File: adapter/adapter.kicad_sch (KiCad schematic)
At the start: 22 parts, among them J1 Serial, J10 Ribbon, J3 Battery charge, J4 RGB, J9 Ribbon, SW1 SW_SPST, SW3 SW_SPDT, U1 Dual MCU: RP2040 + nice!nano, U2 AP1603WG-7

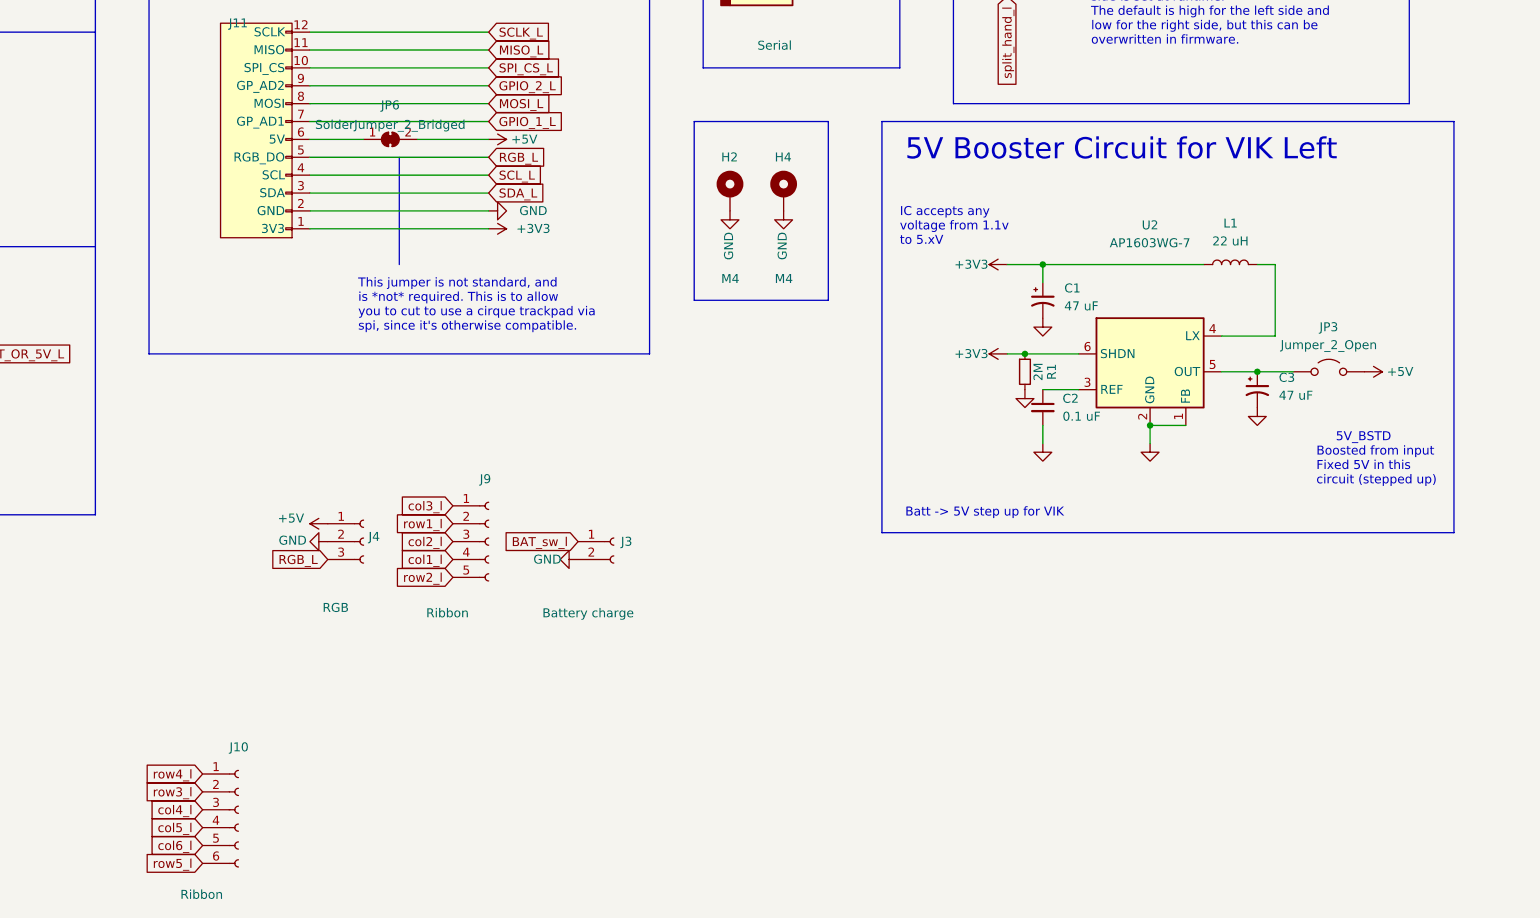
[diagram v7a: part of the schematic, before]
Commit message: sch: remove booster circuit
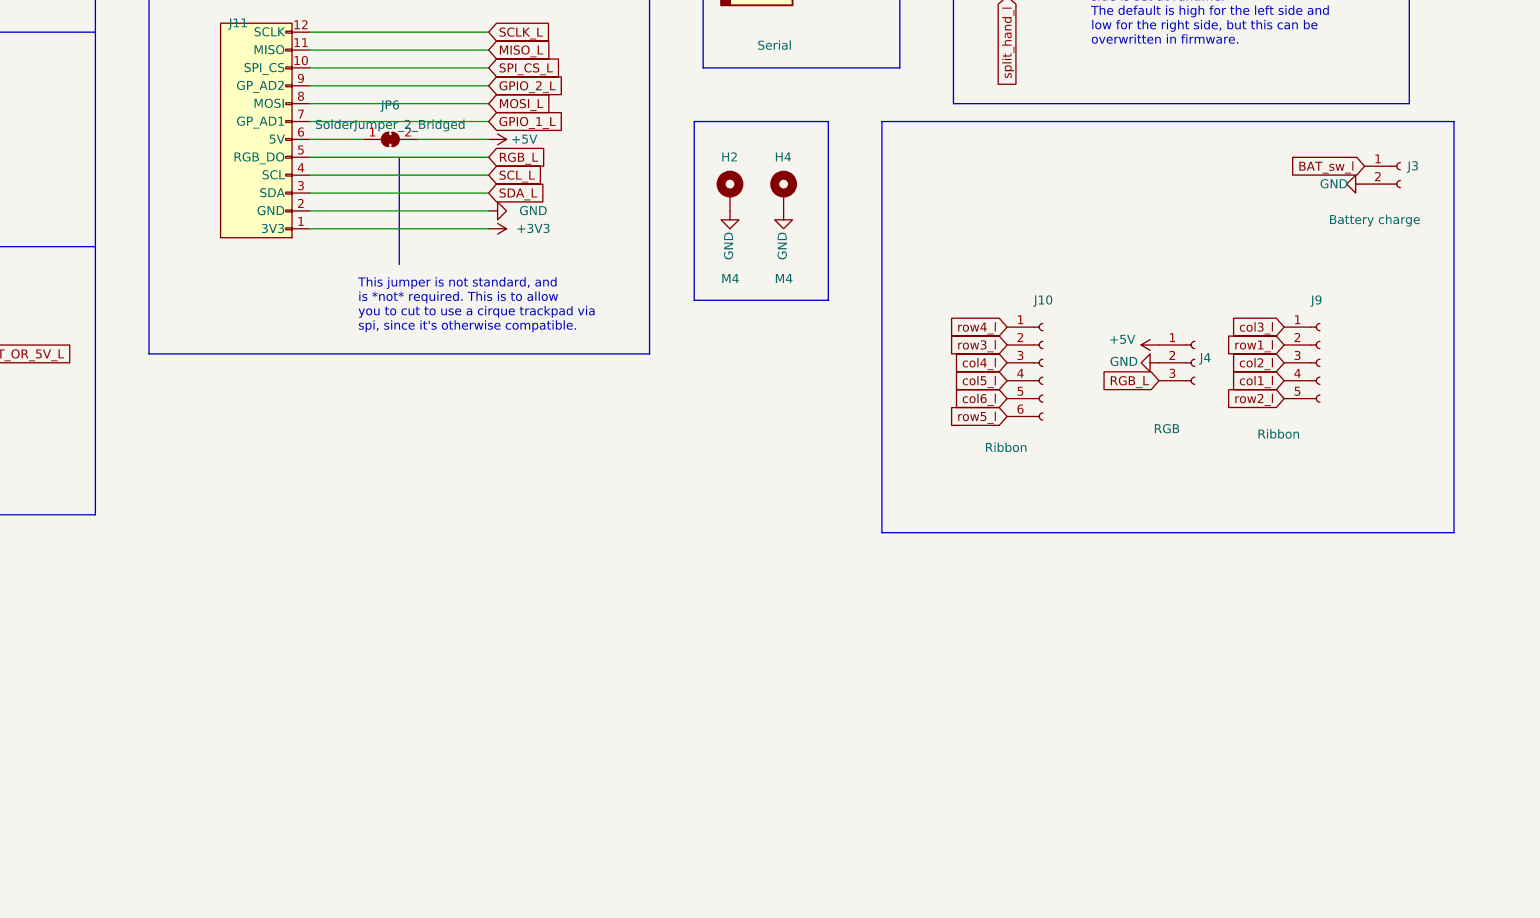
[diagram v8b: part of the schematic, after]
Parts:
- removed C1, C3: 47 uF, Capacitor_SMD:C_0805_2012Metric_Pad1.18x1.45mm_HandSolder, symbol Device:C_Polarized_Small_US
- removed C2: 0.1 uF, Capacitor_SMD:C_0805_2012Metric_Pad1.18x1.45mm_HandSolder, symbol Device:C_Small
- removed JP3: Jumper_2_Open, Jumper:SolderJumper-2_P1.3mm_Open_RoundedPad1.0x1.5mm, symbol Jumper:Jumper_2_Open
- removed L1: 22 uH, Inductor_SMD:L_0805_2012Metric_Pad1.15x1.40mm_HandSolder, symbol Device:L
- removed R1: 2M, Resistor_SMD:R_0805_2012Metric_Pad1.20x1.40mm_HandSolder, symbol Device:R_Small
- removed U2: AP1603WG-7, Package_TO_SOT_SMD:SOT-23-6, symbol AP1603WG-7:AP1603WG-7
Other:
- note removed: "5V Booster Circuit for VIK Left"
- note removed: "5V_BSTD Boosted from input Fixed 5V in this circuit (stepped up)"
- note removed: "Batt -> 5V step up for VIK"
- note removed: "IC accepts any voltage from 1.1v to 5.xV"
- moved on the sheet: J10, J3, J4, J9
